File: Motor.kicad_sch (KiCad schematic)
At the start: 19 parts, among them J3 Screw_Terminal_01x03, U1 MCF8315C1VQRGFRQ1

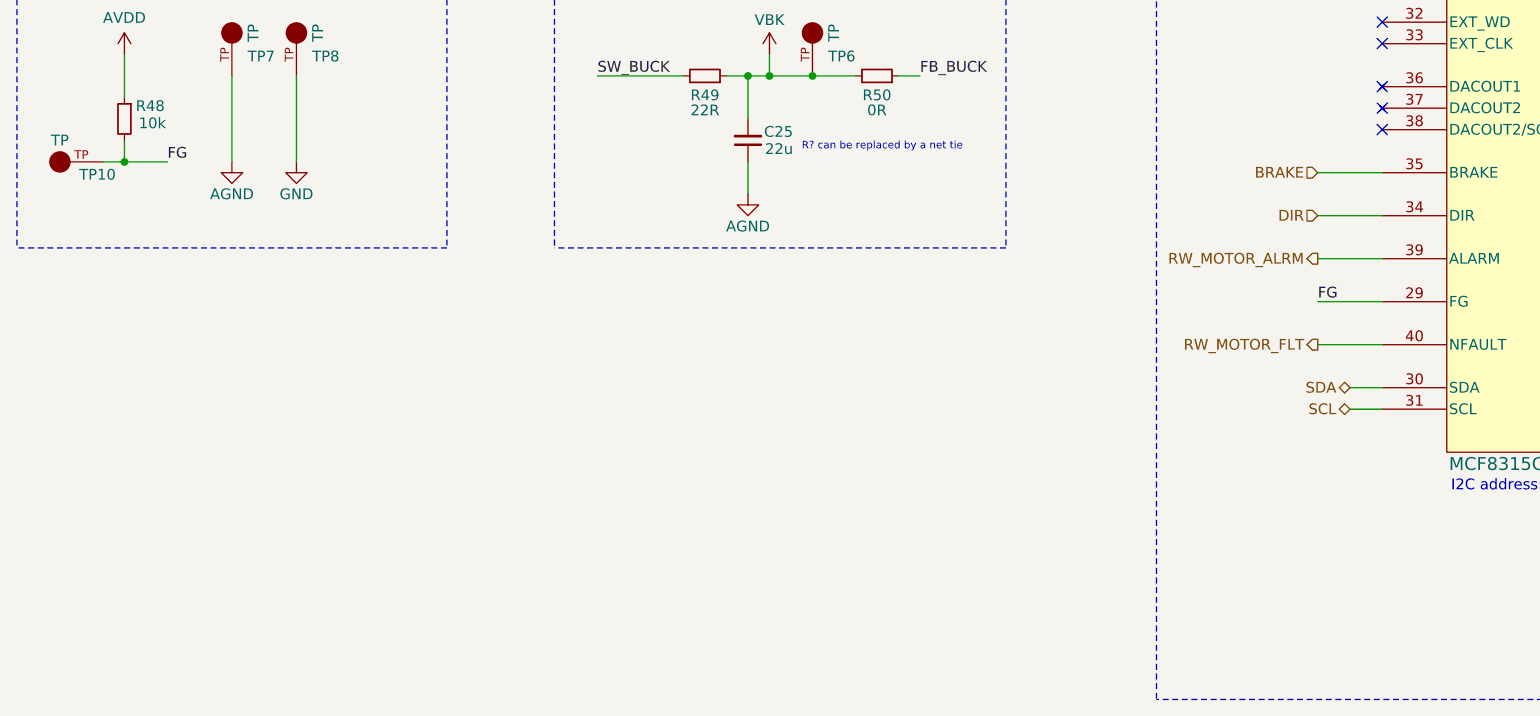
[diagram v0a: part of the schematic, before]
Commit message: moved inductor and added leds
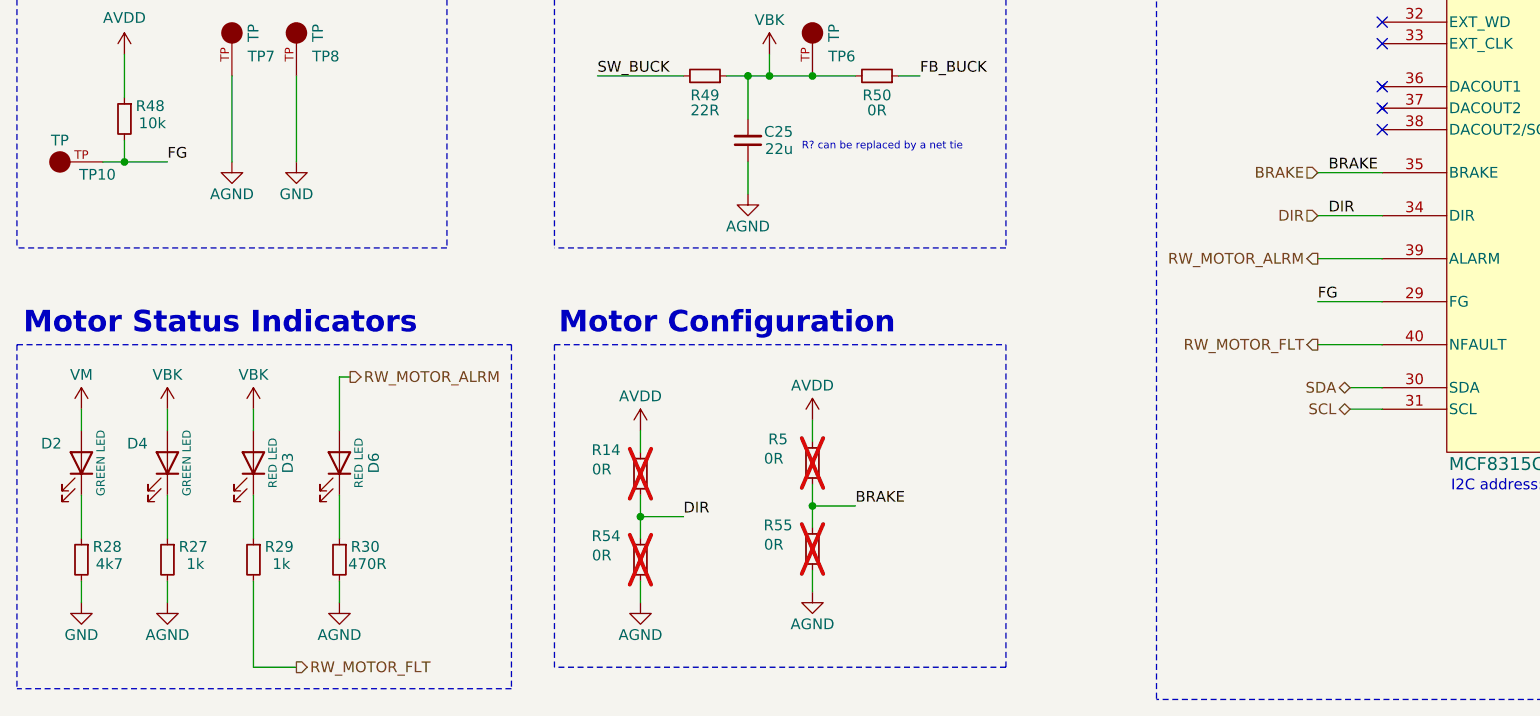
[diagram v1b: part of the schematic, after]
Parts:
- added D2, D4: GREEN LED, LED_SMD:LED_0603_1608Metric, symbol Device:LED
- added D3, D6: RED LED, LED_SMD:LED_0603_1608Metric, symbol Device:LED
- added R14, R5, R54, R55: 0R, Resistor_SMD:R_0402_1005Metric_Pad0.72x0.64mm_HandSolder, symbol Device:R_Small
- added R27, R29: 1k, Resistor_SMD:R_0603_1608Metric, symbol Device:R_Small
- added R28: 4k7, Resistor_SMD:R_0603_1608Metric, symbol Device:R_Small
- added R30: 470R, Resistor_SMD:R_0603_1608Metric, symbol Device:R_Small
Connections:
- net AGND: now also R27.2, R30.2, R54.1, R55.1
- net AVDD: now also R14.2, R5.2
- net BRAKE: now also R5.1, R55.2
- net DIR: now also R14.1, R54.2
- net GND: now also R28.2
- net RW_MOTOR_ALRM: now also D6.2 (A)
- net RW_MOTOR_FLT: now also R29.2
- net VBK: now also D3.2 (A), D4.2 (A)
- net VM: now also D2.2 (A)
- new net: D2.1 (K), R28.1
- new net: D3.1 (K), R29.1
- new net: D4.1 (K), R27.1
- new net: D6.1 (K), R30.1
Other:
- note added: "Motor Configuration"
- note added: "Motor Status Indicators"

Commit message: finished board
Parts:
- C35: footprint Capacitor_SMD:C_0402_1005Metric_Pad0.74x0.62mm_HandSolder -> Capacitor_SMD:C_0603_1608Metric
- R14, R5, R54, R55, R58: footprint Resistor_SMD:R_0402_1005Metric_Pad0.72x0.64mm_HandSolder -> Resistor_SMD:R_0603_1608Metric
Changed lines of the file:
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@@
 			)
 		)
-		(property "Footprint" "Resistor_SMD:R_0402_1005Metric_Pad0.72x0.64mm_HandSolder"
+		(property "Footprint" "Resistor_SMD:R_0603_1608Metric"
 			(at 245.11 39.37 0)
 			(effects
@@
 			)
 		)
-		(property "Footprint" "Resistor_SMD:R_0402_1005Metric_Pad0.72x0.64mm_HandSolder"
+		(property "Footprint" "Resistor_SMD:R_0603_1608Metric"
 			(at 119.38 142.24 0)
 			(effects
@@
 			)
 		)
-		(property "Footprint" "Resistor_SMD:R_0402_1005Metric_Pad0.72x0.64mm_HandSolder"
+		(property "Footprint" "Resistor_SMD:R_0603_1608Metric"
 			(at 119.38 132.08 0)
 			(effects
@@
 			)
 		)
-		(property "Footprint" "Resistor_SMD:R_0402_1005Metric_Pad0.72x0.64mm_HandSolder"
+		(property "Footprint" "Resistor_SMD:R_0603_1608Metric"
 			(at 99.06 133.35 0)
 			(effects
@@
 			)
 		)
-		(property "Footprint" "Resistor_SMD:R_0402_1005Metric_Pad0.72x0.64mm_HandSolder"
+		(property "Footprint" "Resistor_SMD:R_0603_1608Metric"
 			(at 99.06 143.51 0)
 			(effects
@@
 			)
 		)
-		(property "Footprint" "Capacitor_SMD:C_0402_1005Metric_Pad0.74x0.62mm_HandSolder"
+		(property "Footprint" "Capacitor_SMD:C_0603_1608Metric"
 			(at 55.88 40.64 0)
 			(effects
